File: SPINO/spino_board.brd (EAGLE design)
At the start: 100 x 80 mm, 22 parts, among them IC1 ATMEGA168-20P, Q1 16M

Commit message: done SPINO
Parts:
- moved C2 12.7 mm to (24.1, 39.4)
- moved RESET 2.22 mm to (16.8, 39.4)
- moved C5 0.90 mm to (40.0, 17.1)
- moved C4 0.71 mm to (57.8, 17.5)
- moved Q1 0.71 mm to (50.5, 18.4)
- moved R3 0.64 mm to (22.2, 25.4)
- moved R4 0.63 mm to (19.7, 25.4)
- moved C3 0.32 mm to (43.2, 17.5)
- moved R1 0.32 mm to (19.1, 33.3)
- turned JP1 to 180 degrees
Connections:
- removed net N$32: C2.2, IC1.21, JP4.8, RESET.3, RESET.4
- new net N$2: IC1.21, JP4.7
- net GND: now also C2.2, JP4.8, RESET.3, RESET.4; no longer JP4.7
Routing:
- net GND: track 0.00 -> 222.3 mm
- net N$19: track 0.00 -> 221.0 mm
- net VCC: track 0.00 -> 151.1 mm, vias 0 -> 2
- net N$21: track 0.00 -> 95.3 mm
- net N$5: track 0.00 -> 57.4 mm, vias 0 -> 2
- net N$1: track 0.00 -> 33.9 mm
- net N$17: track 0.00 -> 32.2 mm
- net N$4: track 0.00 -> 31.4 mm
- net N$28: track 0.00 -> 31.4 mm
- net N$18: track 0.00 -> 29.1 mm
- net N$20: track 0.00 -> 20.4 mm
- net N$3: track 0.00 -> 18.7 mm
- net N$16: track 0.00 -> 17.0 mm
- net N$15: track 0.00 -> 14.8 mm
- net N$13: track 0.00 -> 12.7 mm
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- added copper zone on layer 1, net GND
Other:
- board text added: "Datle"

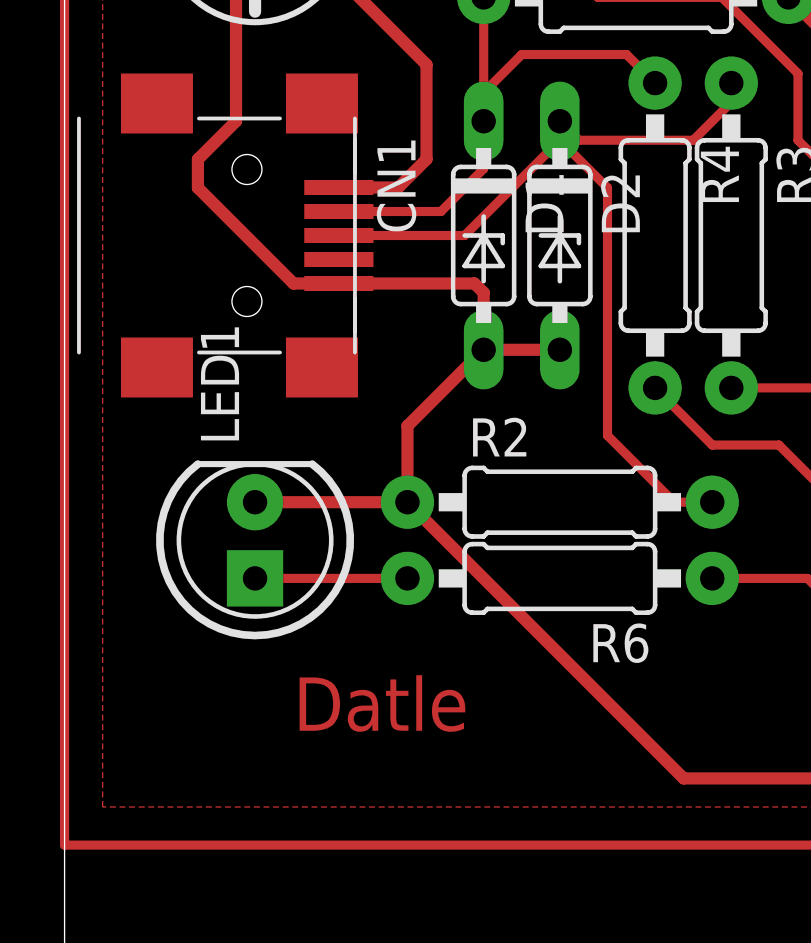
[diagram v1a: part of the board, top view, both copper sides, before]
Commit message: mini usb
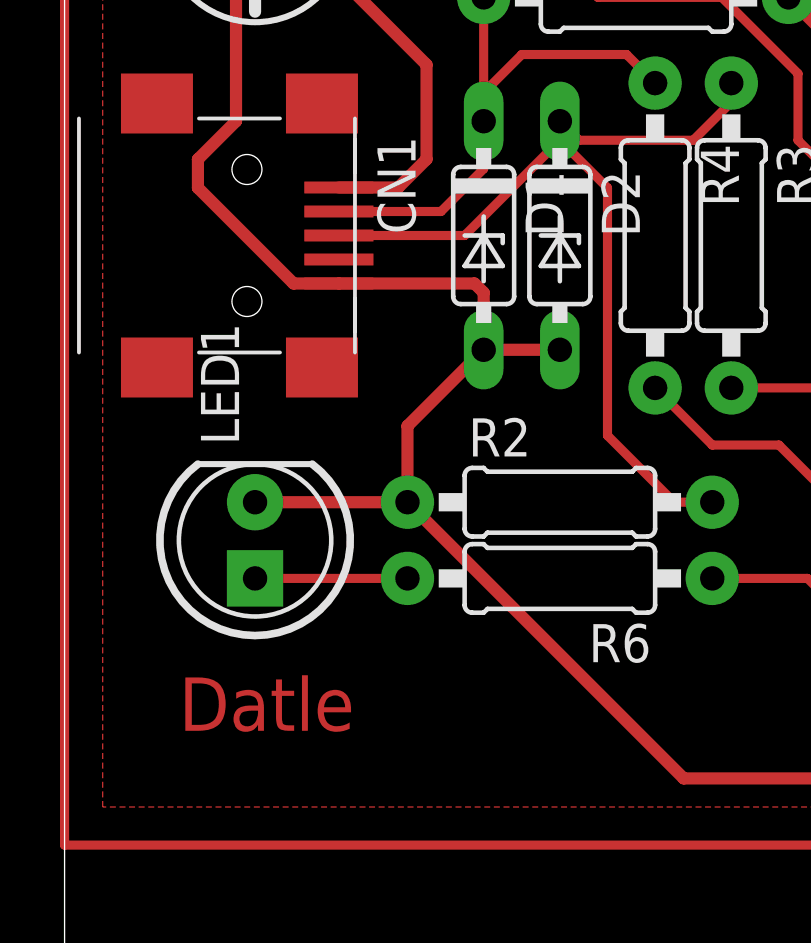
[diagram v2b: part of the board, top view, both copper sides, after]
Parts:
- CN1: device datle-conn:USB-MINIB -> datle-conn:USB-MINIB@1

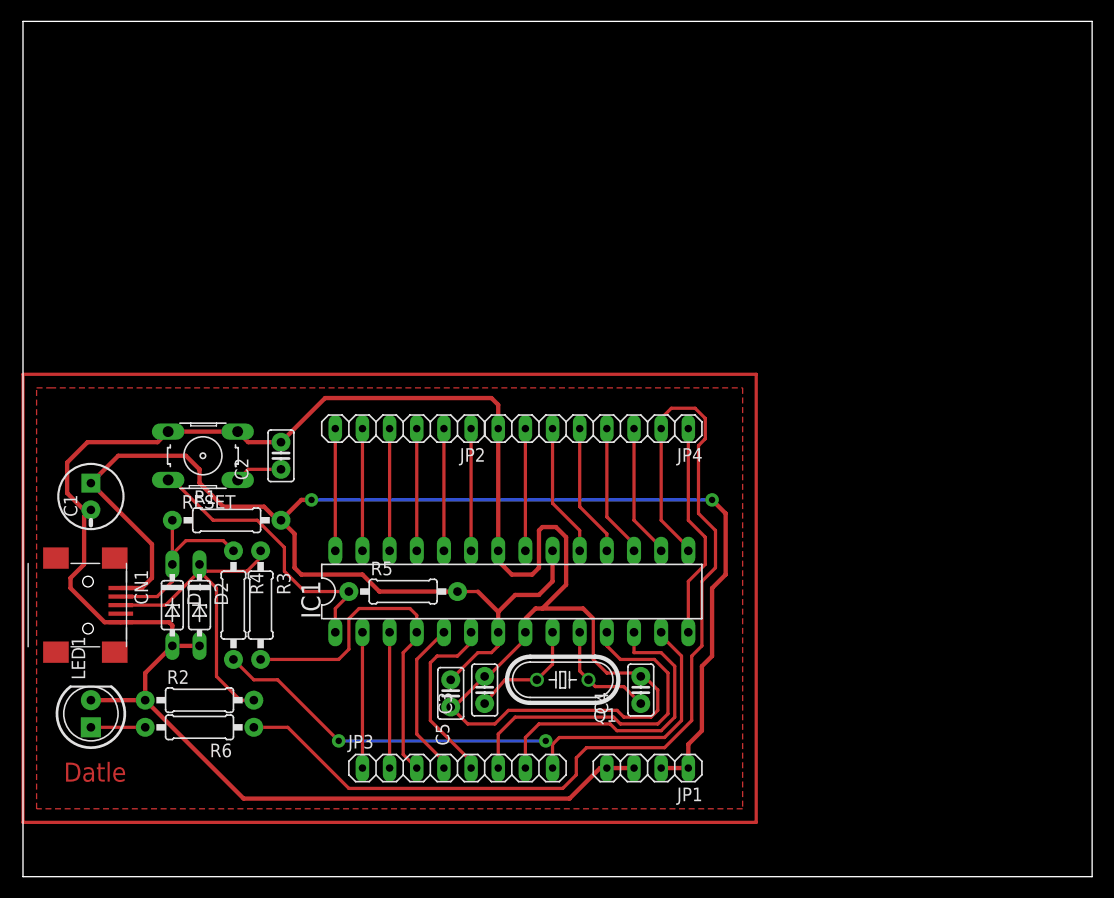
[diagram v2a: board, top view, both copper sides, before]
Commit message: SPINO usb done
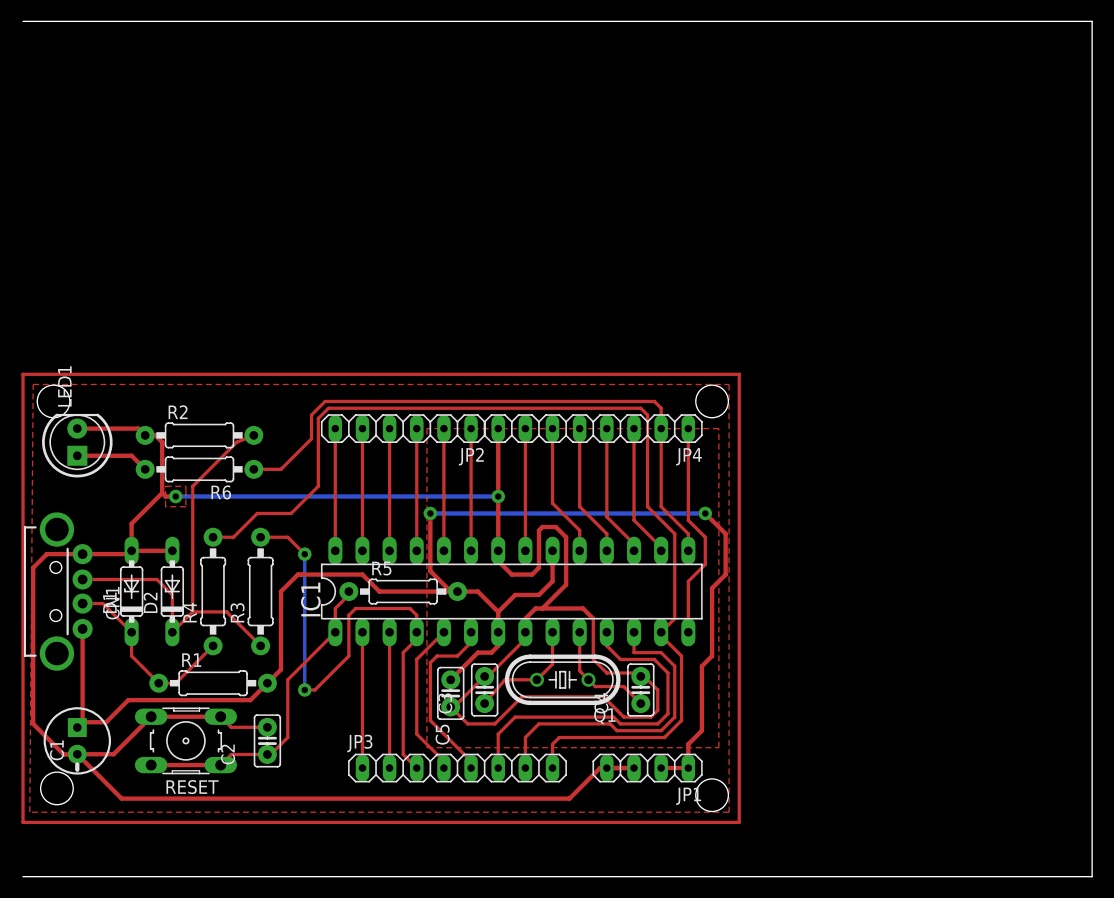
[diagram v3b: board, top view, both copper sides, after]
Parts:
- CN1: value (none) -> USB-2-A-H; device datle-conn:USB-MINIB@1 -> datle-conn:USB-A-H
- moved RESET 26.7 mm to (15.2, 12.7)
- moved C2 26.7 mm to (22.9, 12.7)
- moved LED1 25.4 mm to (5.08, 40.6)
- moved R2 24.8 mm to (16.5, 41.3)
- moved R6 24.1 mm to (16.5, 38.1)
- moved C1 22.9 mm to (5.08, 12.7)
- moved R1 15.3 mm to (17.8, 18.1)
- moved D1 4.02 mm to (10.2, 26.7), turned to 90 degrees
- moved D2 2.84 mm to (14.0, 26.7), turned to 90 degrees
- moved CN1 2.29 mm to (3.17, 26.7), turned to 0 degrees
- moved R4 2.29 mm to (17.8, 26.7), turned to 90 degrees
- moved R3 1.27 mm to (22.2, 26.7), turned to 90 degrees
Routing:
- net N$5: track 57.4 -> 95.8 mm, vias 2 -> 0
- net N$21: track 95.3 -> 57.0 mm
- net GND: track 222.3 -> 245.6 mm, vias 0 -> 2
- net N$1: track 33.9 -> 49.2 mm, vias 0 -> 2
- net VCC: track 151.1 -> 140.2 mm
- net N$4: track 31.4 -> 42.1 mm
- net N$19: track 221.0 -> 217.8 mm
- net N$14: track 5.08 -> 6.88 mm
- net N$28: track 31.4 -> 30.4 mm
- net N$3: track 18.7 -> 18.0 mm
- added copper zone on layer 1, net N$29
- added copper zone on layer 1, net N$30
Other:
- board text removed: "Datle"
